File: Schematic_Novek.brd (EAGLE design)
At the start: 160 x 100 mm, 6 parts, among them IC1 STM32F10XCXT6

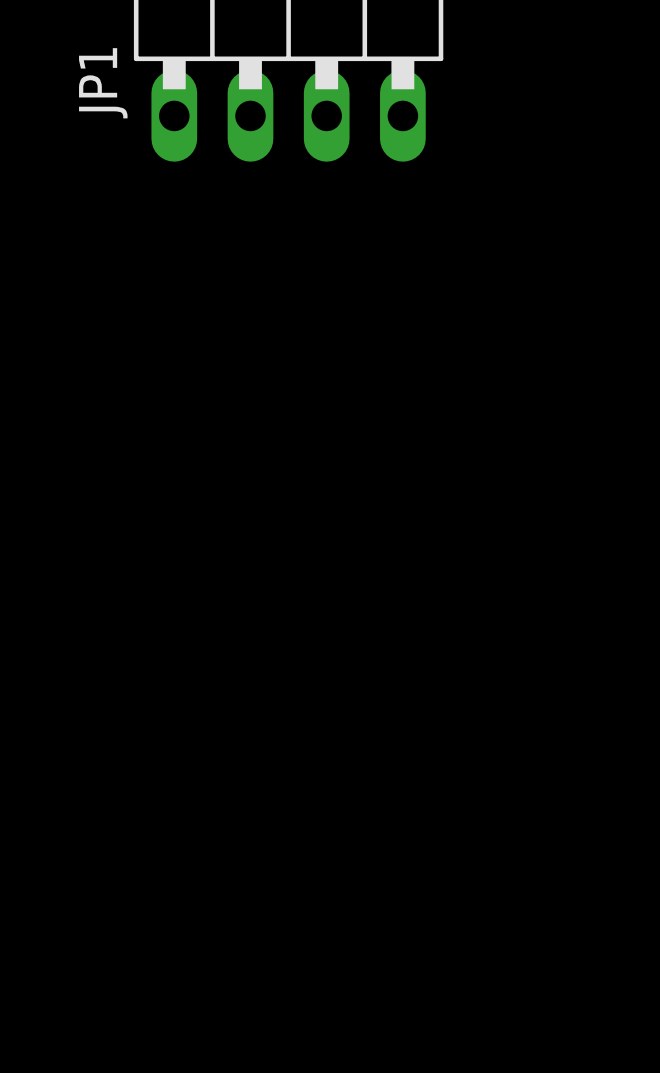
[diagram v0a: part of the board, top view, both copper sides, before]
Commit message: Adds reset and power connections to uC
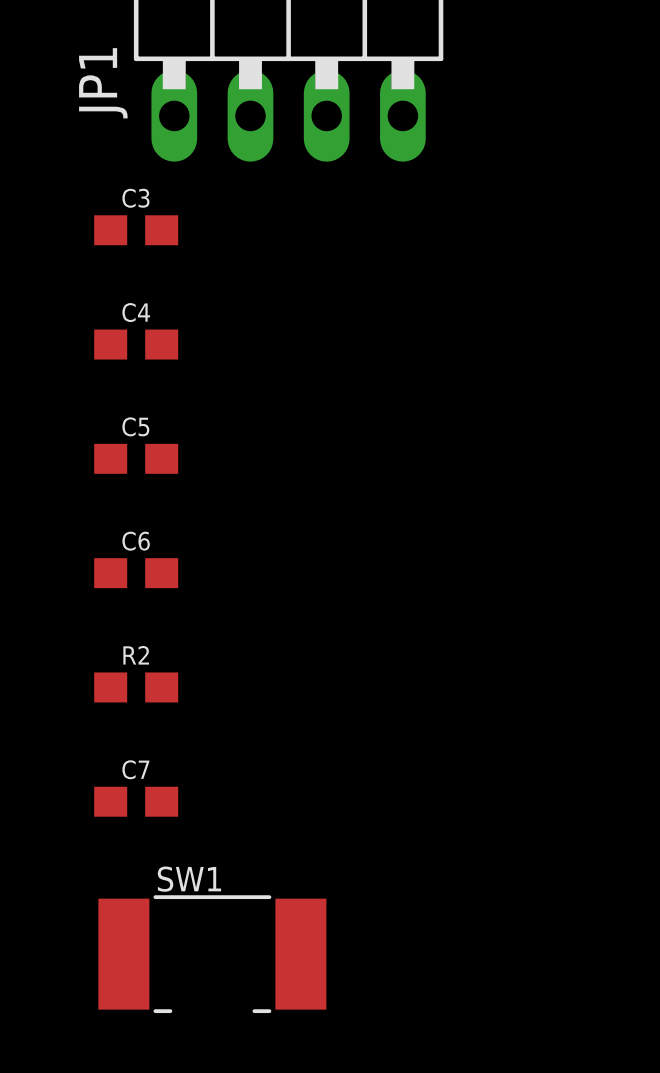
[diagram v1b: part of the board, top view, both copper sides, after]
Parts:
- added C3, C4, C5, C6: 0.1uF, SparkFun-Capacitors:0603
- added C7: 1.0uF, SparkFun-Capacitors:0603
- added R2: 10k, SparkFun-Resistors:0603
- added SW1: (no value), adafruit:BTN_CK_KSS
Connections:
- removed net VDDA: IC1.9
- removed net VDD_1: IC1.24
- removed net VDD_2: IC1.36
- removed net VDD_3: IC1.48
- removed net VSSA: IC1.8
- removed net VSS_1: IC1.23
- removed net VSS_2: IC1.35
- removed net VSS_3: IC1.47
- new net 3.3V: C3.1, C4.1, C5.1, C6.1, IC1.24, IC1.36, IC1.48, IC1.9, R2.2
- new net N$1: C7.2, R2.1, SW1.P$1
- new net N$2: IC1.7
- net GND: now also C3.2, C4.2, C5.2, C6.2, C7.1, IC1.23, IC1.35, IC1.47, IC1.8, SW1.P$2
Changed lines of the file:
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@@
 <layer number="230" name="230bmp" color="7" fill="1" visible="yes" active="yes"/>
 <layer number="231" name="231bmp" color="7" fill="1" visible="yes" active="yes"/>
+<layer number="232" name="Eagle3D_PG2" color="7" fill="1" visible="yes" active="yes"/>
+<layer number="233" name="Eagle3D_PG3" color="7" fill="1" visible="yes" active="yes"/>
 <layer number="248" name="Housing" color="7" fill="1" visible="yes" active="yes"/>
 <layer number="249" name="Edge" color="7" fill="1" visible="yes" active="yes"/>
@@
 <attribute name="VALUE" x="14.605" y="-42.545" size="1.27" layer="27" rot="R90"/>
 </element>
+<element name="C3" library="SparkFun-Capacitors" package="0603" value="0.1uF" x="2.54" y="-45.72" smashed="yes">
+<attribute name="NAME" x="2.54" y="-44.958" size="0.6096" layer="25" font="vector" ratio="20" align="bottom-center"/>
+<attribute name="PROD_ID" value="CAP-00810" x="2.54" y="-45.72" size="1.778" layer="27" display="off"/>
+<attribute name="VALUE" x="2.54" y="-46.482" size="0.6096" layer="27" font="vector" ratio="20" align="top-center"/>
+</element>
+<element name="C4" library="SparkFun-Capacitors" package="0603" value="0.1uF" x="2.54" y="-49.53" smashed="yes">
+<attribute name="NAME" x="2.54" y="-48.768" size="0.6096" layer="25" font="vector" ratio="20" align="bottom-center"/>
+<attribute name="PROD_ID" value="CAP-00810" x="2.54" y="-49.53" size="1.778" layer="27" display="off"/>
+<attribute name="VALUE" x="2.54" y="-50.292" size="0.6096" layer="27" font="vector" ratio="20" align="top-center"/>
+</element>
+<element name="C5" library="SparkFun-Capacitors" package="0603" value="0.1uF" x="2.54" y="-53.34" smashed="yes">
+<attribute name="NAME" x="2.54" y="-52.578" size="0.6096" layer="25" font="vector" ratio="20" align="bottom-center"/>
+<attribute name="PROD_ID" value="CAP-00810" x="2.54" y="-53.34" size="1.778" layer="27" display="off"/>
+<attribute name="VALUE" x="2.54" y="-54.102" size="0.6096" layer="27" font="vector" ratio="20" align="top-center"/>
+</element>
+<element name="C6" library="SparkFun-Capacitors" package="0603" value="0.1uF" x="2.54" y="-57.15" smashed="yes">
+<attribute name="NAME" x="2.54" y="-56.388" size="0.6096" layer="25" font="vector" ratio="20" align="bottom-center"/>
+<attribute name="PROD_ID" value="CAP-00810" x="2.54" y="-57.15" size="1.778" layer="27" display="off"/>
+<attribute name="VALUE" x="2.54" y="-57.912" size="0.6096" layer="27" font="vector" ratio="20" align="top-center"/>
+</element>
+<element name="R2" library="SparkFun-Resistors" package="0603" value="10k" x="2.54" y="-60.96" smashed="yes">
+<attribute name="NAME" x="2.54" y="-60.198" size="0.6096" layer="25" font="vector" ratio="20" align="bottom-center"/>
+<attribute name="PROD_ID" value="RES-00824" x="2.54" y="-60.96" size="1.778" layer="27" display="off"/>
+<attribute name="VALUE" x="2.54" y="-61.722" size="0.6096" layer="27" font="vector" ratio="20" align="top-center"/>
+</element>
+<element name="C7" library="SparkFun-Capacitors" package="0603" value="1.0uF" x="2.54" y="-64.77" smashed="yes">
+<attribute name="NAME" x="2.54" y="-64.008" size="0.6096" layer="25" font="vector" ratio="20" align="bottom-center"/>
+<attribute name="PROD_ID" value="CAP-00868" x="2.54" y="-64.77" size="1.778" layer="27" display="off"/>
+<attribute name="VALUE" x="2.54" y="-65.532" size="0.6096" layer="27" font="vector" ratio="20" align="top-center"/>
+</element>
+<element name="SW1" library="adafruit" package="BTN_CK_KSS" value="" x="5.08" y="-69.85" smashed="yes">
+<attribute name="NAME" x="3.194" y="-67.756" size="0.8128" layer="25" ratio="18"/>
+<attribute name="VALUE" x="3.194" y="-68.706" size="0.4064" layer="27" ratio="10"/>
+</element>
 </elements>
 <signals>
-<signal name="VDD_1">
-<contactref element="IC1" pad="24"/>
-</signal>
-<signal name="VDD_2">
-<contactref element="IC1" pad="36"/>
-</signal>
-<signal name="VDD_3">
-<contactref element="IC1" pad="48"/>
-</signal>
-<signal name="VSS_1">
-<contactref element="IC1" pad="23"/>
-</signal>
-<signal name="VSS_2">
-<contactref element="IC1" pad="35"/>
-</signal>
-<signal name="VSS_3">
-<contactref element="IC1" pad="47"/>
-</signal>
 <signal name="VBAT">
 <contactref element="IC1" pad="1"/>
 </signal>
-<signal name="VSSA">
-<contactref element="IC1" pad="8"/>
-</signal>
-<signal name="VDDA">
-<contactref element="IC1" pad="9"/>
-</signal>
 <signal name="OSCIN">
+<contactref element="IC1" pad="5"/>
 <contactref element="Y1" pad="2"/>
 <contactref element="C1" pad="2"/>
 <contactref element="R1" pad="2"/>
-<contactref element="IC1" pad="5"/>
 <wire x1="3.39" y1="-20.32" x2="8.89" y2="-29.21" width="0" layer="19" extent="1-1"/>
 <wire x1="8.763" y1="-15.24" x2="3.39" y2="-20.32" width="0" layer="19" extent="1-1"/>
@@
 </signal>
 <signal name="OSCOUT">
+<contactref element="IC1" pad="6"/>
 <contactref element="Y1" pad="1"/>
+<contactref element="C2" pad="2"/>
 <contactref element="R1" pad="1"/>
-<contactref element="C2" pad="2"/>
-<contactref element="IC1" pad="6"/>
 <wire x1="3.39" y1="-24.13" x2="1.27" y2="-29.21" width="0" layer="19" extent="1-1"/>
 <wire x1="3.937" y1="-15.24" x2="3.39" y2="-24.13" width="0" layer="19" extent="1-1"/>
@@
 <contactref element="C1" pad="1"/>
 <contactref element="C2" pad="1"/>
+<contactref element="C6" pad="2"/>
+<contactref element="C5" pad="2"/>
+<contactref element="C4" pad="2"/>
+<contactref element="C3" pad="2"/>
+<contactref element="IC1" pad="23"/>
+<contactref element="IC1" pad="35"/>
+<contactref element="IC1" pad="47"/>
+<contactref element="IC1" pad="8"/>
+<contactref element="C7" pad="1"/>
+<contactref element="SW1" pad="P$2"/>
+<wire x1="3.39" y1="-57.15" x2="1.69" y2="-64.77" width="0" layer="19" extent="1-1"/>
+<wire x1="3.39" y1="-53.34" x2="3.39" y2="-57.15" width="0" layer="19" extent="1-1"/>
+<wire x1="3.39" y1="-49.53" x2="3.39" y2="-53.34" width="0" layer="19" extent="1-1"/>
+<wire x1="3.39" y1="-45.72" x2="3.39" y2="-49.53" width="0" layer="19" extent="1-1"/>
+<wire x1="8.03" y1="-69.85" x2="1.69" y2="-64.77" width="0" layer="19" extent="1-1"/>
+<wire x1="1.69" y1="-24.13" x2="3.39" y2="-45.72" width="0" layer="19" extent="1-1"/>
 <wire x1="1.69" y1="-20.32" x2="1.69" y2="-24.13" width="0" layer="19" extent="1-1"/>
+<wire x1="7.1" y1="-10.85" x2="1.69" y2="-20.32" width="0" layer="19" extent="1-1"/>
+<wire x1="1.85" y1="-8.6" x2="7.1" y2="-10.85" width="0" layer="19" extent="1-1"/>
+<wire x1="4.1" y1="-1.85" x2="1.85" y2="-8.6" width="0" layer="19" extent="1-1"/>
+<wire x1="10.85" y1="-4.1" x2="4.1" y2="-1.85" width="0" layer="19" extent="1-1"/>
+</signal>
+<signal name="3.3V">
+<contactref element="C6" pad="1"/>
+<contactref element="C5" pad="1"/>
+<contactref element="C4" pad="1"/>
+<contactref element="C3" pad="1"/>
+<contactref element="IC1" pad="24"/>
+<contactref element="IC1" pad="36"/>
+<contactref element="IC1" pad="48"/>
+<contactref element="IC1" pad="9"/>
+<contactref element="R2" pad="2"/>
+<wire x1="1.69" y1="-57.15" x2="3.39" y2="-60.96" width="0" layer="19" extent="1-1"/>
+<wire x1="1.69" y1="-53.34" x2="1.69" y2="-57.15" width="0" layer="19" extent="1-1"/>
+<wire x1="1.69" y1="-49.53" x2="1.69" y2="-53.34" width="0" layer="19" extent="1-1"/>
+<wire x1="1.69" y1="-45.72" x2="1.69" y2="-49.53" width="0" layer="19" extent="1-1"/>
+<wire x1="7.6" y1="-10.85" x2="1.69" y2="-45.72" width="0" layer="19" extent="1-1"/>
+<wire x1="1.85" y1="-9.1" x2="7.6" y2="-10.85" width="0" layer="19" extent="1-1"/>
+<wire x1="3.6" y1="-1.85" x2="1.85" y2="-9.1" width="0" layer="19" extent="1-1"/>
+<wire x1="10.85" y1="-3.6" x2="3.6" y2="-1.85" width="0" layer="19" extent="1-1"/>
+</signal>
+<signal name="N$1">
+<contactref element="R2" pad="1"/>
+<contactref element="C7" pad="2"/>
+<contactref element="SW1" pad="P$1"/>
+<wire x1="3.39" y1="-64.77" x2="2.13" y2="-69.85" width="0" layer="19" extent="1-1"/>
+<wire x1="1.69" y1="-60.96" x2="3.39" y2="-64.77" width="0" layer="19" extent="1-1"/>
+</signal>
+<signal name="N$2">
+<contactref element="IC1" pad="7"/>
 </signal>
 </signals>

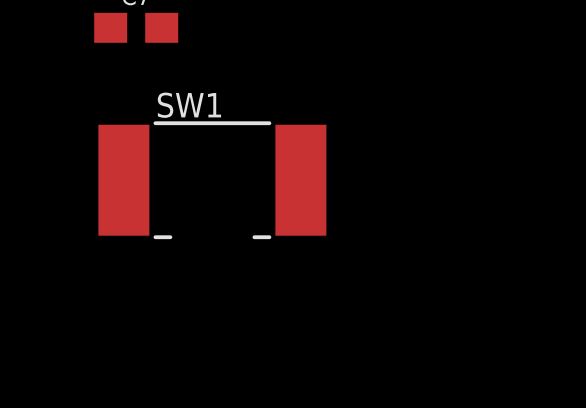
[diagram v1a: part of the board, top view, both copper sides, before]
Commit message: Adds header pin for debugger
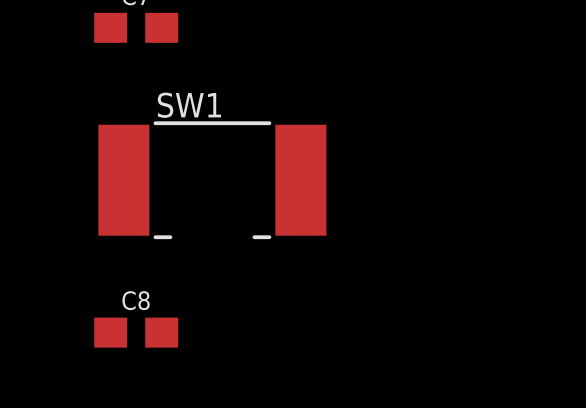
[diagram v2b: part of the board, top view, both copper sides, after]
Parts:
- added C8: 0.1uF, SparkFun-Capacitors:0603
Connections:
- removed net N$1: C7.2, R2.1, SW1.P$1
- removed net N$2: IC1.7
- new net RESET: C7.2, IC1.7, R2.1, SW1.P$1
- new net SWDCLK: IC1.37, JP1.3
- new net SWDIO: IC1.34, JP1.2
- net 3.3V: now also C8.1, JP1.1
- net GND: now also C8.2, JP1.4
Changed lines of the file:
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@@
 <attribute name="VALUE" x="3.194" y="-68.706" size="0.4064" layer="27" ratio="10"/>
+</element>
+<element name="C8" library="SparkFun-Capacitors" package="0603" value="0.1uF" x="2.54" y="-74.93" smashed="yes">
+<attribute name="NAME" x="2.54" y="-74.168" size="0.6096" layer="25" font="vector" ratio="20" align="bottom-center"/>
+<attribute name="PROD_ID" value="CAP-00810" x="2.54" y="-74.93" size="1.778" layer="27" display="off"/>
+<attribute name="VALUE" x="2.54" y="-75.692" size="0.6096" layer="27" font="vector" ratio="20" align="top-center"/>
 </element>
 </elements>
@@
 <contactref element="C7" pad="1"/>
 <contactref element="SW1" pad="P$2"/>
+<contactref element="JP1" pad="4"/>
+<contactref element="C8" pad="2"/>
+<wire x1="8.03" y1="-69.85" x2="3.39" y2="-74.93" width="0" layer="19" extent="1-1"/>
+<wire x1="1.69" y1="-64.77" x2="8.03" y2="-69.85" width="0" layer="19" extent="1-1"/>
 <wire x1="3.39" y1="-57.15" x2="1.69" y2="-64.77" width="0" layer="19" extent="1-1"/>
 <wire x1="3.39" y1="-53.34" x2="3.39" y2="-57.15" width="0" layer="19" extent="1-1"/>
 <wire x1="3.39" y1="-49.53" x2="3.39" y2="-53.34" width="0" layer="19" extent="1-1"/>
 <wire x1="3.39" y1="-45.72" x2="3.39" y2="-49.53" width="0" layer="19" extent="1-1"/>
-<wire x1="8.03" y1="-69.85" x2="1.69" y2="-64.77" width="0" layer="19" extent="1-1"/>
-<wire x1="1.69" y1="-24.13" x2="3.39" y2="-45.72" width="0" layer="19" extent="1-1"/>
+<wire x1="11.43" y1="-41.91" x2="3.39" y2="-45.72" width="0" layer="19" extent="1-1"/>
+<wire x1="1.69" y1="-24.13" x2="11.43" y2="-41.91" width="0" layer="19" extent="1-1"/>
 <wire x1="1.69" y1="-20.32" x2="1.69" y2="-24.13" width="0" layer="19" extent="1-1"/>
 <wire x1="7.1" y1="-10.85" x2="1.69" y2="-20.32" width="0" layer="19" extent="1-1"/>
@@
 <contactref element="IC1" pad="9"/>
 <contactref element="R2" pad="2"/>
+<contactref element="JP1" pad="1"/>
+<contactref element="C8" pad="1"/>
+<wire x1="3.39" y1="-60.96" x2="1.69" y2="-74.93" width="0" layer="19" extent="1-1"/>
 <wire x1="1.69" y1="-57.15" x2="3.39" y2="-60.96" width="0" layer="19" extent="1-1"/>
 <wire x1="1.69" y1="-53.34" x2="1.69" y2="-57.15" width="0" layer="19" extent="1-1"/>
 <wire x1="1.69" y1="-49.53" x2="1.69" y2="-53.34" width="0" layer="19" extent="1-1"/>
 <wire x1="1.69" y1="-45.72" x2="1.69" y2="-49.53" width="0" layer="19" extent="1-1"/>
-<wire x1="7.6" y1="-10.85" x2="1.69" y2="-45.72" width="0" layer="19" extent="1-1"/>
+<wire x1="3.81" y1="-41.91" x2="1.69" y2="-45.72" width="0" layer="19" extent="1-1"/>
+<wire x1="7.6" y1="-10.85" x2="3.81" y2="-41.91" width="0" layer="19" extent="1-1"/>
 <wire x1="1.85" y1="-9.1" x2="7.6" y2="-10.85" width="0" layer="19" extent="1-1"/>
 <wire x1="3.6" y1="-1.85" x2="1.85" y2="-9.1" width="0" layer="19" extent="1-1"/>
 <wire x1="10.85" y1="-3.6" x2="3.6" y2="-1.85" width="0" layer="19" extent="1-1"/>
 </signal>
-<signal name="N$1">
+<signal name="RESET">
+<contactref element="IC1" pad="7"/>
 <contactref element="R2" pad="1"/>
 <contactref element="C7" pad="2"/>
@@
 <wire x1="3.39" y1="-64.77" x2="2.13" y2="-69.85" width="0" layer="19" extent="1-1"/>
 <wire x1="1.69" y1="-60.96" x2="3.39" y2="-64.77" width="0" layer="19" extent="1-1"/>
+<wire x1="6.6" y1="-10.85" x2="1.69" y2="-60.96" width="0" layer="19" extent="1-1"/>
 </signal>
-<signal name="N$2">
-<contactref element="IC1" pad="7"/>
+<signal name="SWDCLK">
+<contactref element="IC1" pad="37"/>
+<contactref element="JP1" pad="3"/>
+<wire x1="1.85" y1="-3.6" x2="8.89" y2="-41.91" width="0" layer="19" extent="1-1"/>
+</signal>
+<signal name="SWDIO">
+<contactref element="IC1" pad="34"/>
+<contactref element="JP1" pad="2"/>
+<wire x1="4.6" y1="-1.85" x2="6.35" y2="-41.91" width="0" layer="19" extent="1-1"/>
 </signal>
 </signals>
